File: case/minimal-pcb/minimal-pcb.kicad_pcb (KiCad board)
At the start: 2 copper layers, 70 x 70 mm, 10 parts, among them J1 USB_C_Receptacle_USB2.0

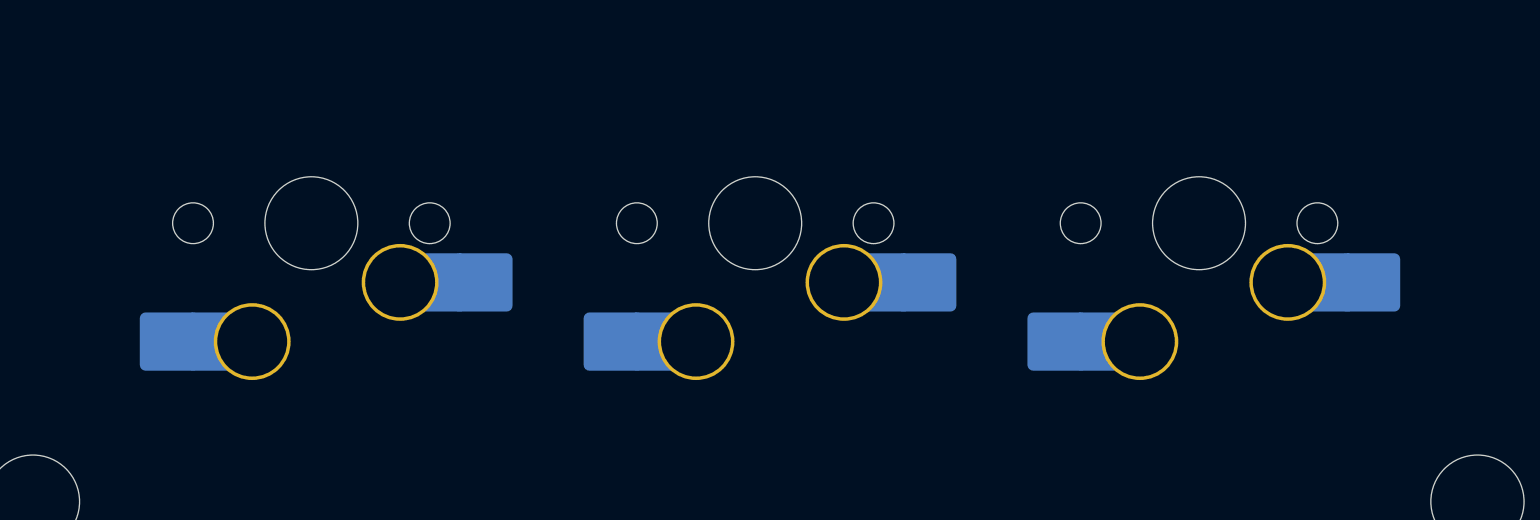
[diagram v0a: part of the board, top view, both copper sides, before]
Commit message: fix: move switches slightly higher, to move away from screw holes
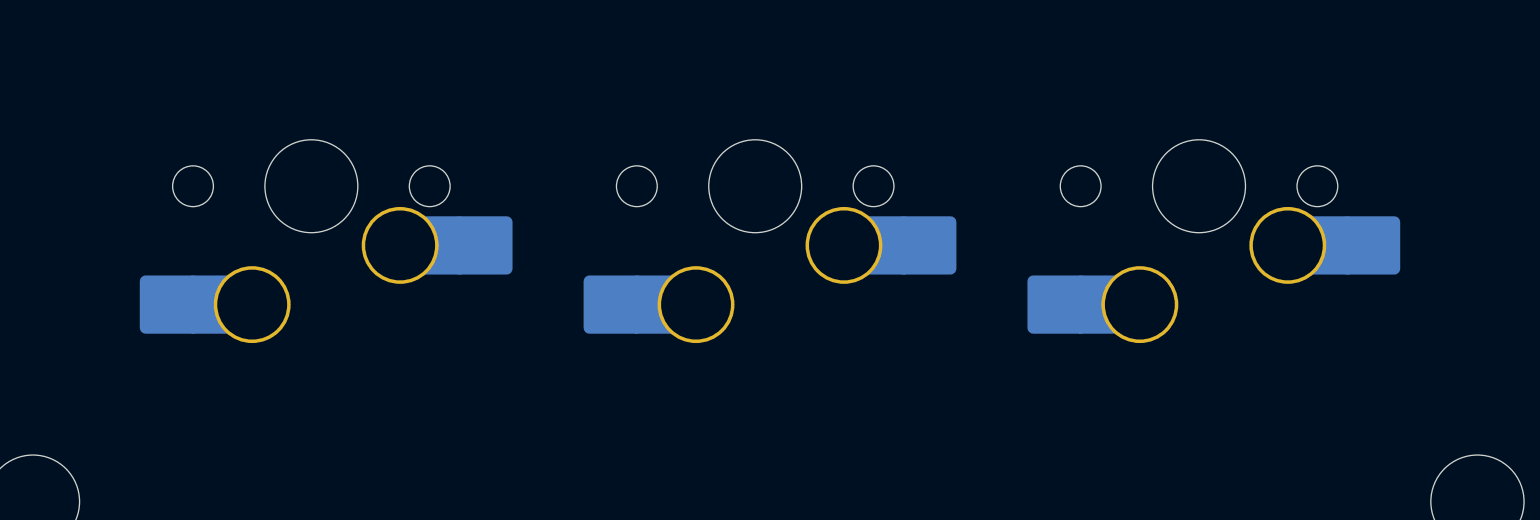
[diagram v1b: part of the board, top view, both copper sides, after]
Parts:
- moved MX1 1.59 mm to (38.1, 74.2)
- moved MX2 1.59 mm to (76.2, 74.2)
- moved MX3 1.59 mm to (57.1, 74.2)
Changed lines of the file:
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@@
   (net 25 "unconnected-(D2-DIN-Pad4)")
   (footprint "PCM_marbastlib-mx:SW_MX_HS_1u" (layer "B.Cu")
-    (at 57.15 75.811647)
+    (at 57.15 74.224147)
     (descr "Footprint for Cherry MX style switches with Kailh hotswap socket")
     (property "Sheetfile" "minimal-pcb.kicad_sch")
@@
   )
   (footprint "PCM_marbastlib-mx:SW_MX_HS_1u" (layer "B.Cu")
-    (at 76.2 75.811647)
+    (at 76.2 74.224147)
     (descr "Footprint for Cherry MX style switches with Kailh hotswap socket")
     (property "Sheetfile" "minimal-pcb.kicad_sch")
@@
   )
   (footprint "PCM_marbastlib-mx:SW_MX_HS_1u" (layer "B.Cu")
-    (at 38.1 75.811647)
+    (at 38.1 74.224147)
     (descr "Footprint for Cherry MX style switches with Kailh hotswap socket")
     (property "Sheetfile" "minimal-pcb.kicad_sch")

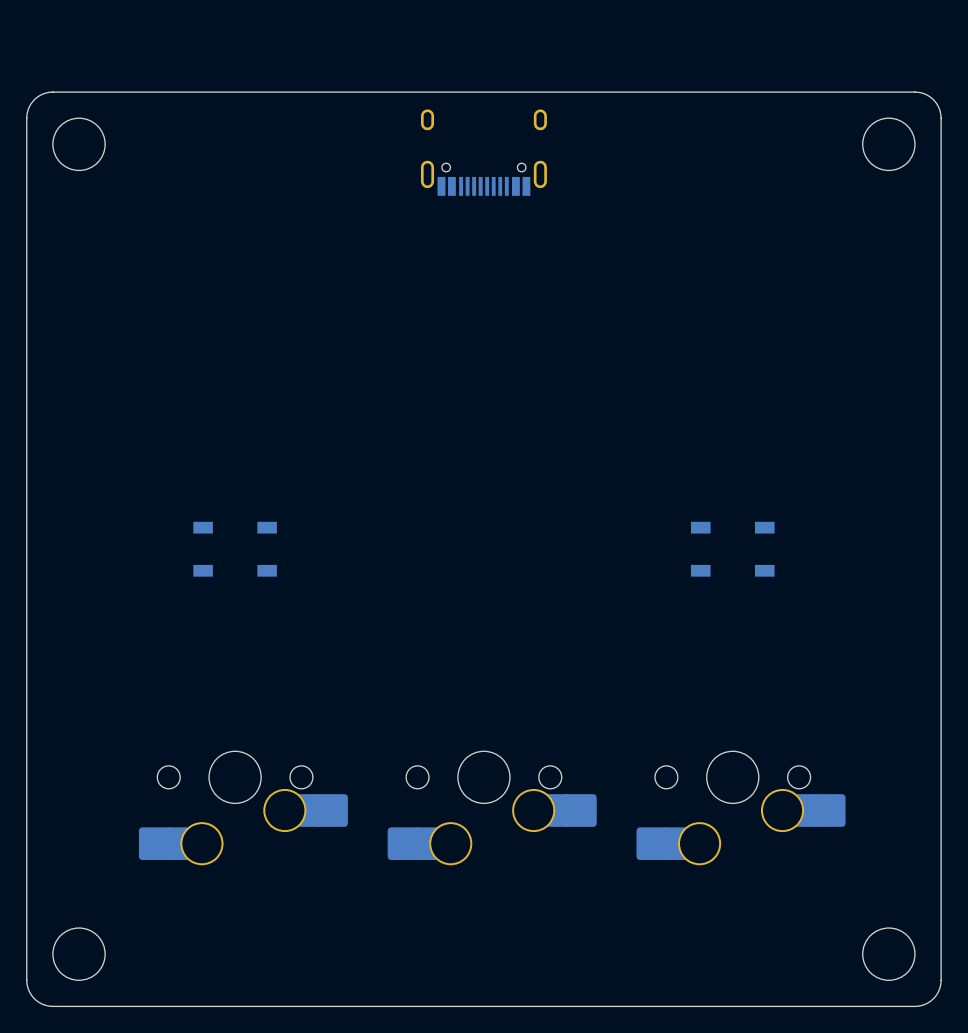
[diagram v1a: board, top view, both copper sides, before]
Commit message: fix: use padded 3.5mm mounting holes in minimal PCB
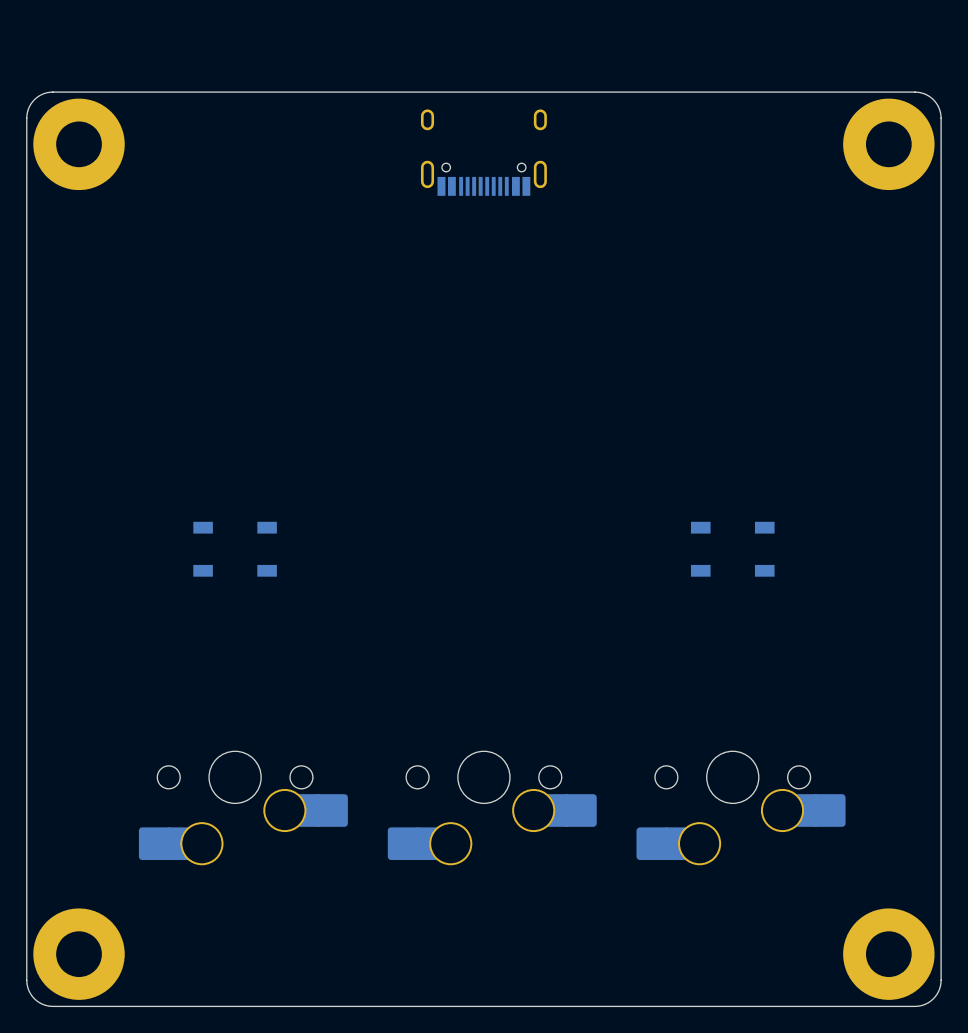
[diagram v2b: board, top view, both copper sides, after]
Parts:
- H1, H2, H3, H4: value 4mm Diameter Mounting Hole -> Mounting Hole; footprint MountingHole:MountingHole_4mm -> MountingHole:MountingHole_3.5mm_Pad
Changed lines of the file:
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@@
     )
   )
-  (footprint "MountingHole:MountingHole_4mm" (layer "B.Cu")
+  (footprint "MountingHole:MountingHole_3.5mm_Pad" (layer "B.Cu")
     (at 88.15 25.761647 180)
-    (descr "Mounting Hole 4mm, no annular")
-    (tags "mounting hole 4mm no annular")
+    (descr "Mounting Hole 3.5mm")
+    (tags "mounting hole 3.5mm")
     (property "Sheetfile" "minimal-pcb.kicad_sch")
     (property "Sheetname" "")
@@
     (property "ki_keywords" "mounting hole")
     (attr exclude_from_pos_files)
-    (fp_text reference "H2" (at 0 5) (layer "B.SilkS")
+    (fp_text reference "H2" (at 0 4.5) (layer "B.SilkS")
         (effects (font (size 1 1) (thickness 0.15)) (justify mirror))
     )
-    (fp_text value "4mm Diameter Mounting Hole" (at 0 -5) (layer "B.Fab")
+    (fp_text value "Mounting Hole" (at 0 -4.5) (layer "B.Fab")
         (effects (font (size 1 1) (thickness 0.15)) (justify mirror))
     )
@@
         (effects (font (size 1 1) (thickness 0.15)) (justify mirror))
     )
-    (fp_circle (center 0 0) (end 4 0)
+    (fp_circle (center 0 0) (end 3.5 0)
       (stroke (width 0.15) (type solid)) (fill none) (layer "Cmts.User"))
-    (fp_circle (center 0 0) (end 4.25 0)
+    (fp_circle (center 0 0) (end 3.75 0)
       (stroke (width 0.05) (type solid)) (fill none) (layer "B.CrtYd"))
-    (pad "" np_thru_hole circle (at 0 0 180) (size 4 4) (drill 4) (layers "*.Cu" "*.Mask"))
+    (pad "1" thru_hole circle (at 0 0 180) (size 7 7) (drill 3.5) (layers "*.Cu" "*.Mask"))
   )
   (footprint "LED_SMD:LED_WS2812B_PLCC4_5.0x5.0mm_P3.2mm" (layer "B.Cu")
@@
     )
   )
-  (footprint "MountingHole:MountingHole_4mm" (layer "B.Cu")
+  (footprint "MountingHole:MountingHole_3.5mm_Pad" (layer "B.Cu")
     (at 88.15 87.761647 180)
-    (descr "Mounting Hole 4mm, no annular")
-    (tags "mounting hole 4mm no annular")
+    (descr "Mounting Hole 3.5mm")
+    (tags "mounting hole 3.5mm")
     (property "Sheetfile" "minimal-pcb.kicad_sch")
     (property "Sheetname" "")
@@
     (property "ki_keywords" "mounting hole")
     (attr exclude_from_pos_files)
-    (fp_text reference "H4" (at 0 5) (layer "B.SilkS")
+    (fp_text reference "H4" (at 0 4.5) (layer "B.SilkS")
         (effects (font (size 1 1) (thickness 0.15)) (justify mirror))
     )
-    (fp_text value "4mm Diameter Mounting Hole" (at 0 -5) (layer "B.Fab")
+    (fp_text value "Mounting Hole" (at 0 -4.5) (layer "B.Fab")
         (effects (font (size 1 1) (thickness 0.15)) (justify mirror))
     )
@@
         (effects (font (size 1 1) (thickness 0.15)) (justify mirror))
     )
-    (fp_circle (center 0 0) (end 4 0)
+    (fp_circle (center 0 0) (end 3.5 0)
       (stroke (width 0.15) (type solid)) (fill none) (layer "Cmts.User"))
-    (fp_circle (center 0 0) (end 4.25 0)
+    (fp_circle (center 0 0) (end 3.75 0)
       (stroke (width 0.05) (type solid)) (fill none) (layer "B.CrtYd"))
-    (pad "" np_thru_hole circle (at 0 0 180) (size 4 4) (drill 4) (layers "*.Cu" "*.Mask"))
+    (pad "1" thru_hole circle (at 0 0 180) (size 7 7) (drill 3.5) (layers "*.Cu" "*.Mask"))
   )
-  (footprint "MountingHole:MountingHole_4mm" (layer "B.Cu")
+  (footprint "MountingHole:MountingHole_3.5mm_Pad" (layer "B.Cu")
     (at 26.15 87.761647 180)
-    (descr "Mounting Hole 4mm, no annular")
-    (tags "mounting hole 4mm no annular")
+    (descr "Mounting Hole 3.5mm")
+    (tags "mounting hole 3.5mm")
     (property "Sheetfile" "minimal-pcb.kicad_sch")
     (property "Sheetname" "")
@@
     (property "ki_keywords" "mounting hole")
     (attr exclude_from_pos_files)
-    (fp_text reference "H3" (at 0 5) (layer "B.SilkS")
+    (fp_text reference "H3" (at 0 4.5) (layer "B.SilkS")
         (effects (font (size 1 1) (thickness 0.15)) (justify mirror))
     )
-    (fp_text value "4mm Diameter Mounting Hole" (at 0 -5) (layer "B.Fab")
+    (fp_text value "Mounting Hole" (at 0 -4.5) (layer "B.Fab")
         (effects (font (size 1 1) (thickness 0.15)) (justify mirror))
     )
@@
         (effects (font (size 1 1) (thickness 0.15)) (justify mirror))
     )
-    (fp_circle (center 0 0) (end 4 0)
+    (fp_circle (center 0 0) (end 3.5 0)
       (stroke (width 0.15) (type solid)) (fill none) (layer "Cmts.User"))
-    (fp_circle (center 0 0) (end 4.25 0)
+    (fp_circle (center 0 0) (end 3.75 0)
       (stroke (width 0.05) (type solid)) (fill none) (layer "B.CrtYd"))
-    (pad "" np_thru_hole circle (at 0 0 180) (size 4 4) (drill 4) (layers "*.Cu" "*.Mask"))
+    (pad "1" thru_hole circle (at 0 0 180) (size 7 7) (drill 3.5) (layers "*.Cu" "*.Mask"))
   )
-  (footprint "MountingHole:MountingHole_4mm" (layer "B.Cu")
+  (footprint "MountingHole:MountingHole_3.5mm_Pad" (layer "B.Cu")
     (at 26.15 25.761647 180)
-    (descr "Mounting Hole 4mm, no annular")
-    (tags "mounting hole 4mm no annular")
+    (descr "Mounting Hole 3.5mm")
+    (tags "mounting hole 3.5mm")
     (property "Sheetfile" "minimal-pcb.kicad_sch")
     (property "Sheetname" "")
@@
     (property "ki_keywords" "mounting hole")
     (attr exclude_from_pos_files)
-    (fp_text reference "H1" (at 0 5) (layer "B.SilkS")
+    (fp_text reference "H1" (at 0 4.5) (layer "B.SilkS")
         (effects (font (size 1 1) (thickness 0.15)) (justify mirror))
     )
-    (fp_text value "4mm Diameter Mounting Hole" (at 0 -5) (layer "B.Fab")
+    (fp_text value "Mounting Hole" (at 0 -4.5) (layer "B.Fab")
         (effects (font (size 1 1) (thickness 0.15)) (justify mirror))
     )
@@
         (effects (font (size 1 1) (thickness 0.15)) (justify mirror))
     )
-    (fp_circle (center 0 0) (end 4 0)
+    (fp_circle (center 0 0) (end 3.5 0)
       (stroke (width 0.15) (type solid)) (fill none) (layer "Cmts.User"))
-    (fp_circle (center 0 0) (end 4.25 0)
+    (fp_circle (center 0 0) (end 3.75 0)
       (stroke (width 0.05) (type solid)) (fill none) (layer "B.CrtYd"))
-    (pad "" np_thru_hole circle (at 0 0 180) (size 4 4) (drill 4) (layers "*.Cu" "*.Mask"))
+    (pad "1" thru_hole circle (at 0 0 180) (size 7 7) (drill 3.5) (layers "*.Cu" "*.Mask"))
   )
   (footprint "PCM_marbastlib-various:USB_C_Receptacle_HRO_TYPE-C-31-M-12" (layer "B.Cu")
